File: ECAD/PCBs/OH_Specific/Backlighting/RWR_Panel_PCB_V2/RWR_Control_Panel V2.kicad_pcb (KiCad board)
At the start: 2 copper layers, 93 x 40.6 mm, 35 parts, among them J1 BL IN, J2 BL OUT, J3 SWITCH BUTTONS, P3 CONN_01X01, P4 CONN_01X01, P5 CONN_01X01, P6 CONN_01X01, SW1 BIT, SW2 OFFSET, SW3 SPECIAL, SW4 LIMIT, SW5 POWER

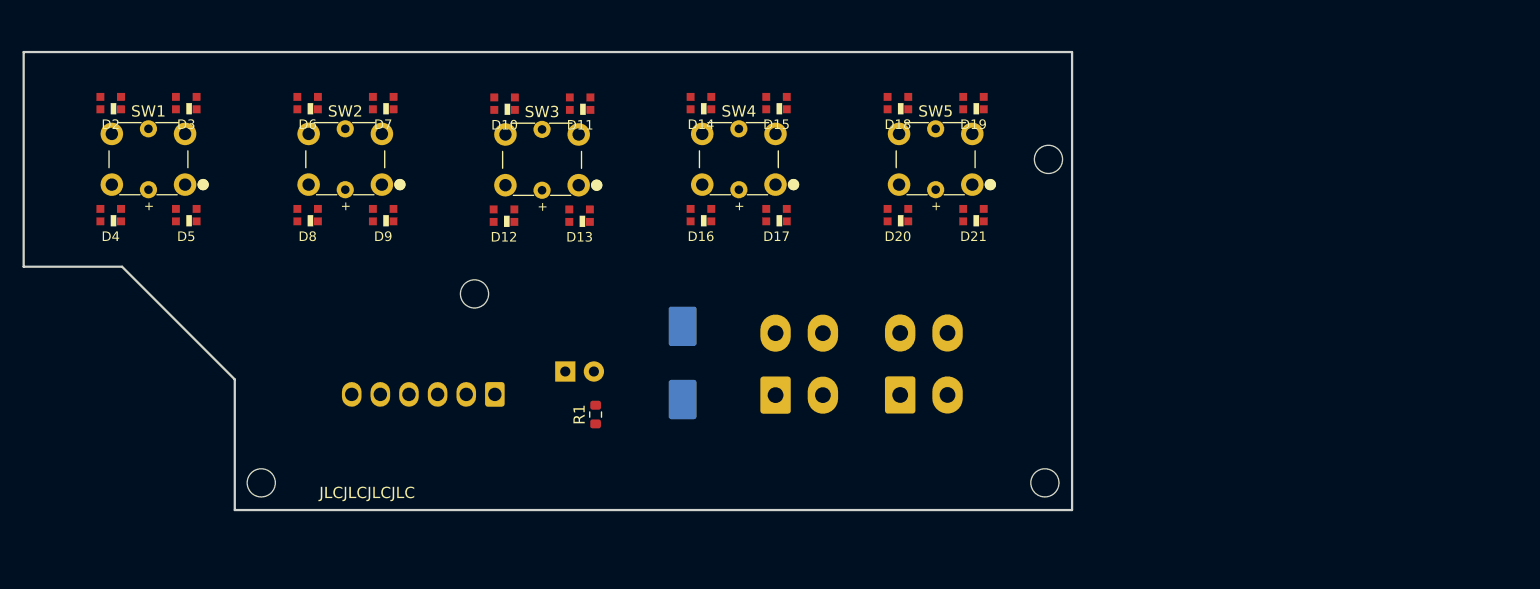
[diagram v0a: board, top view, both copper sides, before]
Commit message: Updated RWR Control Panel on LIP
Added BL to panel legends, and reorgnized outputs on the PCB.

RWR Panel is "done".
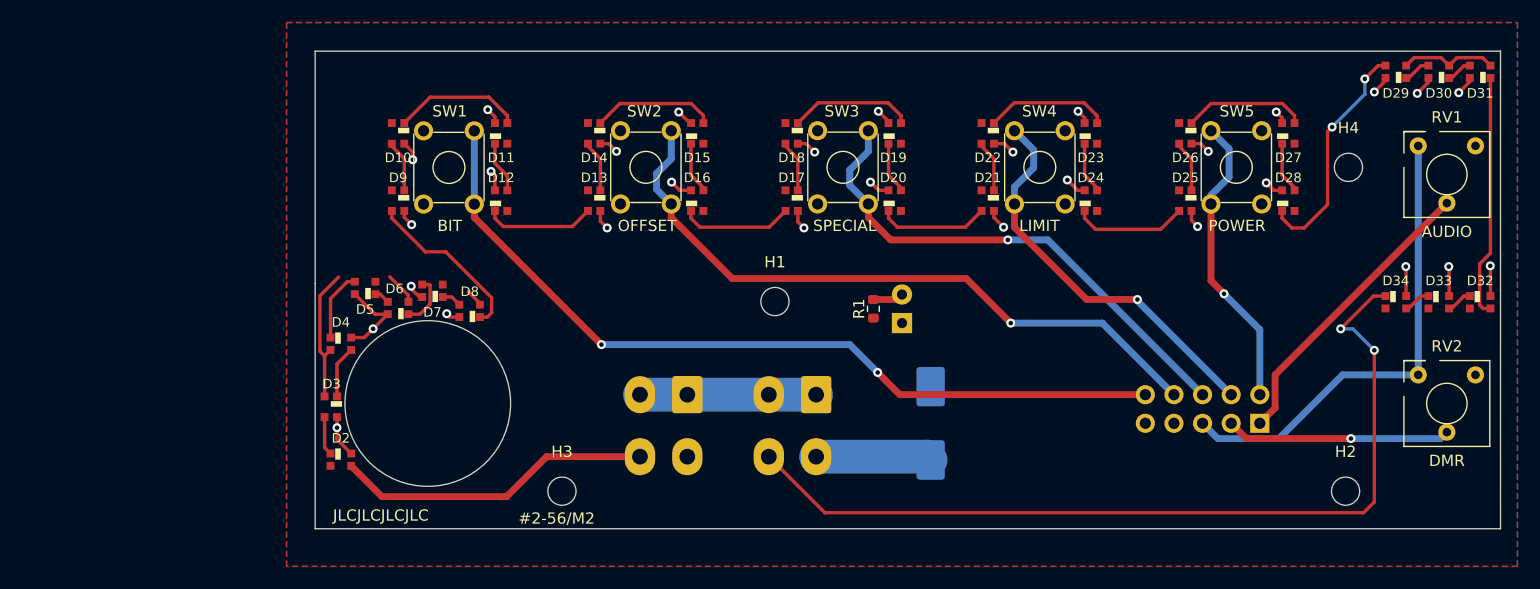
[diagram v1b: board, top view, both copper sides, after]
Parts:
- removed P3, P4, P5, P6: CONN_01X01, MountingHole:MountingHole_2.5mm
- added D22: LED, KiCAD Libraries:WS2812-2020, F.Cu at (186.4, 88.9)
- added D23: LED, KiCAD Libraries:WS2812-2020, F.Cu at (195.6, 88.9)
- added D24: LED, KiCAD Libraries:WS2812-2020, F.Cu at (195.6, 94.9)
- added D25: LED, KiCAD Libraries:WS2812-2020, F.Cu at (203.9, 94.9)
- added D26: LED, KiCAD Libraries:WS2812-2020, F.Cu at (203.9, 88.9)
- added D27: LED, KiCAD Libraries:WS2812-2020, F.Cu at (213.1, 88.9)
- added D28: LED, KiCAD Libraries:WS2812-2020, F.Cu at (213.1, 94.9)
- added D29: LED, KiCAD Libraries:WS2812-2020, F.Cu at (222.6, 83.4)
- added D30: LED, KiCAD Libraries:WS2812-2020, F.Cu at (226.4, 83.4)
- added D31: LED, KiCAD Libraries:WS2812-2020, F.Cu at (230.1, 83.4)
- added D32: LED, KiCAD Libraries:WS2812-2020, F.Cu at (230.1, 103.9)
- added D33: LED, KiCAD Libraries:WS2812-2020, F.Cu at (226.4, 103.9)
- added D34: LED, KiCAD Libraries:WS2812-2020, F.Cu at (222.6, 103.9)
- added H1: MountingHole, MountingHole:MountingHole_2.5mm, F.Cu at (167.5, 103.8)
- added H2: MountingHole, MountingHole:MountingHole_2.5mm, F.Cu at (218.2, 120.7)
- added H3: MountingHole, MountingHole:MountingHole_2.5mm, F.Cu at (148.6, 120.7)
- added H4: MountingHole, MountingHole:MountingHole_2.5mm, F.Cu at (218.4, 91.9)
- added RV1: AUDIO, KiCAD Libraries:Bourns_3310Y, F.Cu at (227.2, 92.6)
- added RV2: DMR, KiCAD Libraries:Bourns_3310Y, F.Cu at (227.2, 112.9)
- D10, D11, D12, D13, D14, D15, D16, D17, D18, D19, D2, D20, D21, D3, D4, D5, D6, D7, D8, D9: footprint OH_KiCAD_Libraries:WS2812-2020 -> KiCAD Libraries:WS2812-2020
- J3: value SWITCH BUTTONS -> INPUTS; footprint Connector_Molex:Molex_KK-254_AE-6410-06A_1x06_P2.54mm_Vertical -> Connector_PinHeader_2.54mm:PinHeader_2x05_P2.54mm_Vertical
- SW1, SW2, SW3, SW4, SW5: footprint OH_KiCAD_Libraries:TL1240GQ -> Button_Switch_THT:SW_TH_Tactile_Omron_B3F-10xx
- moved J3 67.9 mm to (210.6, 114.6), turned to 90 degrees
- moved D2 37.7 mm to (129.0, 117.9), turned to 180 degrees
- moved SW3 32.2 mm to (175.8, 88.7), turned to 270 degrees
- moved SW2 32.2 mm to (158.3, 88.7), turned to 270 degrees
- moved SW1 32.2 mm to (140.9, 88.7), turned to 270 degrees
- moved D1 30.2 mm to (178.8, 105.7), turned to 90 degrees
- moved D3 29.8 mm to (128.1, 113.2), turned to 90 degrees
- moved SW4 28.4 mm to (188.8, 95.2), turned to 90 degrees
- moved SW5 28.4 mm to (206.2, 95.2), turned to 90 degrees
- moved R1 26.4 mm to (176.3, 104.5), turned to 270 degrees
- moved D4 23.4 mm to (129.0, 107.6), turned to 180 degrees
- moved C1 22.6 mm to (181.3, 114.6), turned to 270 degrees
- moved D6 19.9 mm to (134.1, 104.4)
- moved J1 18.9 mm to (159.8, 112.1), turned to 180 degrees
- moved D7 17.2 mm to (137.1, 102.9)
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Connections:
- C1 pad 1: /LED+5V -> /BL_+5V
- D1 pad 1: /LED+5V -> /BL_+5V
- D10 pad 1: /LED+5V -> Net-(D10-Pad1)
- D10 pad 2: Net-(D10-Pad2) -> GND
- D10 pad 3: GND -> /BL_DATA1
- D10 pad 4: Net-(D10-Pad4) -> /BL_+5V
- D11 pad 1: /LED+5V -> Net-(D11-Pad1)
- D11 pad 2: Net-(D11-Pad2) -> GND
- D11 pad 3: GND -> Net-(D10-Pad1)
- D11 pad 4: Net-(D10-Pad2) -> /BL_+5V
- D12 pad 1: /LED+5V -> Net-(D12-Pad1)
- D12 pad 2: Net-(D12-Pad2) -> GND
- D12 pad 3: GND -> Net-(D11-Pad1)
- D12 pad 4: Net-(D11-Pad2) -> /BL_+5V
- D13 pad 1: /LED+5V -> Net-(D13-Pad1)
- D13 pad 2: Net-(D13-Pad2) -> GND
- D13 pad 3: GND -> Net-(D12-Pad1)
- D13 pad 4: Net-(D12-Pad2) -> /BL_+5V
- D14 pad 1: /LED+5V -> Net-(D14-Pad1)
- D14 pad 2: Net-(D14-Pad2) -> GND
- D14 pad 3: GND -> Net-(D13-Pad1)
- D14 pad 4: Net-(D13-Pad2) -> /BL_+5V
- D15 pad 1: /LED+5V -> Net-(D15-Pad1)
- D15 pad 2: Net-(D15-Pad2) -> GND
- D15 pad 3: GND -> Net-(D14-Pad1)
- D15 pad 4: Net-(D14-Pad2) -> /BL_+5V
- D16 pad 1: /LED+5V -> Net-(D16-Pad1)
- D16 pad 2: Net-(D16-Pad2) -> GND
- D16 pad 3: GND -> Net-(D15-Pad1)
- D16 pad 4: Net-(D15-Pad2) -> /BL_+5V
- D17 pad 1: /LED+5V -> /BL_DATA2
- D17 pad 2: Net-(D17-Pad2) -> GND
- D17 pad 3: GND -> Net-(D16-Pad1)
- D17 pad 4: Net-(D16-Pad2) -> /BL_+5V
- D18 pad 1: /LED+5V -> Net-(D18-Pad1)
- D18 pad 2: Net-(D18-Pad2) -> GND
- D18 pad 3: GND -> /BL_DATA2
- D18 pad 4: Net-(D17-Pad2) -> /BL_+5V
- D19 pad 1: /LED+5V -> Net-(D19-Pad1)
- D19 pad 2: Net-(D19-Pad2) -> GND
- D19 pad 3: GND -> Net-(D18-Pad1)
- D19 pad 4: Net-(D18-Pad2) -> /BL_+5V
- D2 pad 1: /LED+5V -> Net-(D2-Pad1)
- D2 pad 2: Net-(D2-Pad2) -> GND
- D2 pad 3: GND -> /BL_DIN
- D2 pad 4: /LEDDATAIN -> /BL_+5V
- D20 pad 1: /LED+5V -> Net-(D20-Pad1)
- D20 pad 2: Net-(D20-Pad2) -> GND
- D20 pad 3: GND -> Net-(D19-Pad1)
- D20 pad 4: Net-(D19-Pad2) -> /BL_+5V
- D21 pad 1: /LED+5V -> Net-(D21-Pad1)
- D21 pad 2: /LEDDATAOUT -> GND
- D21 pad 3: GND -> Net-(D20-Pad1)
- D21 pad 4: Net-(D20-Pad2) -> /BL_+5V
- D3 pad 1: /LED+5V -> Net-(D3-Pad1)
- D3 pad 2: Net-(D3-Pad2) -> GND
- D3 pad 3: GND -> Net-(D2-Pad1)
- D3 pad 4: Net-(D2-Pad2) -> /BL_+5V
- D4 pad 1: /LED+5V -> Net-(D4-Pad1)
- D4 pad 2: Net-(D4-Pad2) -> GND
- D4 pad 3: GND -> Net-(D3-Pad1)
- D4 pad 4: Net-(D3-Pad2) -> /BL_+5V
- D5 pad 1: /LED+5V -> Net-(D5-Pad1)
- D5 pad 2: Net-(D5-Pad2) -> GND
- D5 pad 3: GND -> Net-(D4-Pad1)
- D5 pad 4: Net-(D4-Pad2) -> /BL_+5V
- D6 pad 1: /LED+5V -> Net-(D6-Pad1)
- D6 pad 2: Net-(D6-Pad2) -> GND
- D6 pad 3: GND -> Net-(D5-Pad1)
- D6 pad 4: Net-(D5-Pad2) -> /BL_+5V
- D7 pad 1: /LED+5V -> Net-(D7-Pad1)
- D7 pad 2: Net-(D7-Pad2) -> GND
- D7 pad 3: GND -> Net-(D6-Pad1)
- D7 pad 4: Net-(D6-Pad2) -> /BL_+5V
- D8 pad 1: /LED+5V -> Net-(D8-Pad1)
- D8 pad 2: Net-(D8-Pad2) -> GND
- D8 pad 3: GND -> Net-(D7-Pad1)
- D8 pad 4: Net-(D7-Pad2) -> /BL_+5V
- D9 pad 1: /LED+5V -> /BL_DATA1
- D9 pad 2: Net-(D10-Pad4) -> GND
- D9 pad 3: GND -> Net-(D8-Pad1)
- D9 pad 4: Net-(D8-Pad2) -> /BL_+5V
- J1 pad 1: /LED+5V -> /BL_+5V
- J1 pad 2: /LED+5V -> /BL_+5V
- J1 pad 4: /LEDDATAIN -> /BL_DIN
- J2 pad 1: /LED+5V -> /BL_+5V
- J2 pad 2: /LED+5V -> /BL_+5V
- J2 pad 4: /LEDDATAOUT -> /BL_DOUT
- J3 pad 1: /BIT_SW -> /A_AUDIO
- J3 pad 2: /OFFSET_SW -> /POWER_SW
- J3 pad 3: /SPECIAL_SW -> /A_DMR
- J3 pad 5: /POWER_SW -> +5V
- J3 pad 6: GND -> /SPECIAL_SW
- SW1 pad 2: GND -> /BIT_SW
- SW1 pad 3: (no net) -> GND
- SW1 pad 4: (no net) -> GND
- SW2 pad 2: GND -> /OFFSET_SW
- SW2 pad 3: (no net) -> GND
- SW2 pad 4: (no net) -> GND
- SW3 pad 2: GND -> /SPECIAL_SW
- SW3 pad 3: (no net) -> GND
- SW3 pad 4: (no net) -> GND
- SW4 pad 2: GND -> /LIMIT_SW
- SW4 pad 3: (no net) -> GND
- SW4 pad 4: (no net) -> GND
- SW5 pad 2: GND -> /POWER_SW
- SW5 pad 3: (no net) -> GND
- SW5 pad 4: (no net) -> GND
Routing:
- net /BL_DOUT: track 0.00 -> 78.6 mm, vias 0 -> 2
- net /BL_+5V: track 0.00 -> 76.5 mm, vias 0 -> 30
- net /BIT_SW: track 0.00 -> 73.7 mm, vias 0 -> 2
- net /OFFSET_SW: track 0.00 -> 59.9 mm, vias 0 -> 1
- net /SPECIAL_SW: track 0.00 -> 45.2 mm, vias 0 -> 1
- net +5V: track 0.00 -> 42.4 mm
- net GND: track 0.00 -> 35.6 mm
- net /LIMIT_SW: track 0.00 -> 35.4 mm, vias 0 -> 1
- net /BL_DIN: track 0.00 -> 28.2 mm
- net /POWER_SW: track 0.00 -> 26.5 mm, vias 0 -> 1
- net /A_AUDIO: track 0.00 -> 26.4 mm
- net Net-(D31-Pad1): track 0.00 -> 21.6 mm
- net Net-(D28-Pad1): track 0.00 -> 21.0 mm, vias 0 -> 2
- net /A_DMR: track 0.00 -> 19.9 mm, vias 0 -> 1
- net Net-(D8-Pad1): track 0.00 -> 15.0 mm
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- added copper zone on B.Cu, net /BL_+5V
- added copper zone on F.Cu, net GND
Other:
- board size 93 x 40.6 mm -> 105.2 x 42.4 mm
- board text added: "#2-56/M2"
- board text added: "Version 2.5"
- board text removed: "H1"
- board text removed: "H2"
- board text removed: "H3"
- board text removed: "H4"
- board text removed: "RWR Panel Designed by L. Walker"
- board text removed: "Version 2.0"
- board text removed: "⌀2-32 2MM"
